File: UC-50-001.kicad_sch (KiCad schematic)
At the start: 0 parts

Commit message: RAM : temporairement fini
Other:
- sheet RAM renamed I02–05–07–08–09–11–12–17–19–23–RAM
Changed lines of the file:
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@@
     (stroke (width 0.1524) (type solid) (color 0 0 0 0))
     (fill (color 0 0 0 0.0000))
-    (property "Sheet name" "RAM" (id 0) (at 30.48 76.4934 0)
+    (property "Sheet name" "I02–05–07–08–09–11–12–17–19–23–RAM" (id 0) (at 30.48 76.4934 0)
       (effects (font (size 1.8 1.8)) (justify left bottom))
     )
@@
       (reference "#PWR?") (unit 1) (value "GND") (footprint "")
     )
+    (path "/3b9df46e-3592-4470-9765-1c36c3c4b1c2/0c08bfbe-48ca-4db2-92f3-dc7b8238d261"
+      (reference "#PWR?") (unit 1) (value "GND") (footprint "")
+    )
     (path "/f465a4b1-7c3c-40cc-9e66-ff9f17003d42/0f6a8f7c-8ebc-48ff-a299-e91c43441b34"
       (reference "#PWR?") (unit 1) (value "GND") (footprint "")
@@
       (reference "#PWR?") (unit 1) (value "+5V") (footprint "")
     )
+    (path "/3b9df46e-3592-4470-9765-1c36c3c4b1c2/7435153a-c468-4d7b-8502-3365d7ea767d"
+      (reference "#PWR?") (unit 1) (value "+5V") (footprint "")
+    )
     (path "/afd59d07-bfd6-4bc9-8176-e0ddec1872a1/76921501-701f-4c1f-8225-7bfdc888d467"
       (reference "#PWR?") (unit 1) (value "GND") (footprint "")
@@
       (reference "#PWR?") (unit 1) (value "GND") (footprint "")
     )
+    (path "/3b9df46e-3592-4470-9765-1c36c3c4b1c2/89541933-c7ab-4d42-acee-72bf689ebaa3"
+      (reference "#PWR?") (unit 1) (value "GND") (footprint "")
+    )
     (path "/b7e71b61-5858-491f-a12d-087d8cf2d648/8bd665a3-d2bc-4eb9-ab07-d1b073552cd5"
       (reference "#PWR?") (unit 1) (value "+5V") (footprint "")
@@
       (reference "#PWR?") (unit 1) (value "GND") (footprint "")
     )
+    (path "/3b9df46e-3592-4470-9765-1c36c3c4b1c2/9b2f435e-c9f5-4022-a643-0a2a885f898c"
+      (reference "#PWR?") (unit 1) (value "GND") (footprint "")
+    )
     (path "/afd59d07-bfd6-4bc9-8176-e0ddec1872a1/9b9e676b-a45e-44f0-8f14-e409b9618c02"
       (reference "#PWR?") (unit 1) (value "GND") (footprint "")
     )
+    (path "/3b9df46e-3592-4470-9765-1c36c3c4b1c2/9bd4cdcc-9b91-440c-8f95-cc6edf9cc717"
+      (reference "#PWR?") (unit 1) (value "+5V") (footprint "")
+    )
     (path "/3b9df46e-3592-4470-9765-1c36c3c4b1c2/a00adc77-b775-4350-9b35-84be2bc872bc"
       (reference "#PWR?") (unit 1) (value "GND") (footprint "")
@@
       (reference "#PWR?") (unit 1) (value "+5V") (footprint "")
     )
+    (path "/3b9df46e-3592-4470-9765-1c36c3c4b1c2/bd8749e0-1840-4927-bb4e-27bf2d69b91e"
+      (reference "#PWR?") (unit 1) (value "+5V") (footprint "")
+    )
     (path "/3b9df46e-3592-4470-9765-1c36c3c4b1c2/bde68ce5-ebc7-4aa3-8add-c6386f0e31b1"
       (reference "#PWR?") (unit 1) (value "GND") (footprint "")
@@
       (reference "#PWR?") (unit 1) (value "+5V") (footprint "")
     )
+    (path "/3b9df46e-3592-4470-9765-1c36c3c4b1c2/c8f86357-7c56-49dd-841f-0b8016155e76"
+      (reference "#PWR?") (unit 1) (value "GND") (footprint "")
+    )
     (path "/b7e71b61-5858-491f-a12d-087d8cf2d648/cc2f772d-66f5-4ef2-bf72-bf4cabe8468e"
       (reference "#PWR?") (unit 1) (value "GND") (footprint "")
@@
     )
     (path "/3b9df46e-3592-4470-9765-1c36c3c4b1c2/d74e7404-2964-4604-a79a-633d2f0c5c76"
+      (reference "#PWR?") (unit 1) (value "GND") (footprint "")
+    )
+    (path "/3b9df46e-3592-4470-9765-1c36c3c4b1c2/d85bd63e-ddec-4520-b1c2-47b8d0d2c25a"
+      (reference "#PWR?") (unit 1) (value "GND") (footprint "")
+    )
+    (path "/3b9df46e-3592-4470-9765-1c36c3c4b1c2/dd1a7648-1801-4481-97bd-fb427a294716"
       (reference "#PWR?") (unit 1) (value "GND") (footprint "")
     )
@@
       (reference "C01") (unit 1) (value "100uF") (footprint "")
     )
+    (path "/3b9df46e-3592-4470-9765-1c36c3c4b1c2/e7011fa1-0a2a-4048-a729-5a3912728b22"
+      (reference "C02") (unit 1) (value "100pF") (footprint "")
+    )
+    (path "/3b9df46e-3592-4470-9765-1c36c3c4b1c2/5c0ace55-ad46-4721-b2a9-13c47105194e"
+      (reference "C03") (unit 1) (value "100pF") (footprint "")
+    )
     (path "/b7e71b61-5858-491f-a12d-087d8cf2d648/36dce4c7-2705-4bcb-b676-3fb13d1e9187"
       (reference "C7") (unit 1) (value "220nF") (footprint "")
@@
       (reference "C31") (unit 1) (value "47nF") (footprint "")
     )
+    (path "/3b9df46e-3592-4470-9765-1c36c3c4b1c2/df1775be-95fd-4d6c-9689-ecaeb7ae759a"
+      (reference "C33") (unit 1) (value "47nF") (footprint "")
+    )
     (path "/3b9df46e-3592-4470-9765-1c36c3c4b1c2/04c98286-549c-4582-8a40-dd933b3c8a44"
       (reference "C35") (unit 1) (value "47nF") (footprint "")
@@
       (reference "C?") (unit 1) (value "100uF") (footprint "")
     )
+    (path "/3b9df46e-3592-4470-9765-1c36c3c4b1c2/4393184f-e494-46f3-b5c4-6143e8e72043"
+      (reference "C?") (unit 1) (value "47nF") (footprint "")
+    )
     (path "/3b9df46e-3592-4470-9765-1c36c3c4b1c2/76e33095-d5c1-4315-9b36-4ce1828dbef6"
       (reference "C?") (unit 1) (value "10nF") (footprint "")
@@
       (reference "C?") (unit 1) (value "47nF") (footprint "")
     )
-    (path "/3b9df46e-3592-4470-9765-1c36c3c4b1c2/df1775be-95fd-4d6c-9689-ecaeb7ae759a"
+    (path "/3b9df46e-3592-4470-9765-1c36c3c4b1c2/f3d75b2b-a10e-400b-95b7-25d1a994b88f"
       (reference "C?") (unit 1) (value "47nF") (footprint "")
     )
@@
       (reference "I08") (unit 1) (value "TMS4416 – 16k×4bits DRAM") (footprint "Package_DIP:DIP-18_W7.62mm_LongPads")
     )
+    (path "/3b9df46e-3592-4470-9765-1c36c3c4b1c2/e5b33663-4b58-4516-8cd9-ab2a59a9d103"
+      (reference "I09") (unit 1) (value "74LS32 – 4× 2-input OR gates") (footprint "Package_DIP:DIP-14_W7.62mm_LongPads")
+    )
     (path "/3b9df46e-3592-4470-9765-1c36c3c4b1c2/edf7d0d1-1070-4c87-a709-1d85f3bb622c"
       (reference "I11") (unit 1) (value "TMS4416 – 16k×4bits DRAM") (footprint "Package_DIP:DIP-18_W7.62mm_LongPads")
     )
+    (path "/3b9df46e-3592-4470-9765-1c36c3c4b1c2/5544af09-10f1-4418-a4ab-05a6362d4390"
+      (reference "I12") (unit 1) (value "74LS11 – 3×3 inputs AND gates") (footprint "Package_DIP:DIP-14_W7.62mm_LongPads")
+    )
     (path "/3b9df46e-3592-4470-9765-1c36c3c4b1c2/72e2b5de-308f-467f-abcc-77d273bcfa07"
       (reference "I17") (unit 1) (value "74LS245 – Bus transceiver") (footprint "Package_DIP:DIP-20_W7.62mm_LongPads")
@@
       (reference "R13") (unit 1) (value "3K3") (footprint "")
     )
+    (path "/3b9df46e-3592-4470-9765-1c36c3c4b1c2/7cc7717b-b384-4c56-8c71-316373184291"
+      (reference "R29") (unit 1) (value "100") (footprint "")
+    )
     (path "/f465a4b1-7c3c-40cc-9e66-ff9f17003d42/86aa1ccc-5151-4ba7-a26f-79b9e96ed260"
       (reference "R31") (unit 1) (value "1K") (footprint "")
@@
       (reference "R33") (unit 1) (value "1K") (footprint "")
     )
+    (path "/3b9df46e-3592-4470-9765-1c36c3c4b1c2/9c7d7f95-2f97-474d-ae54-bf4c023ef25b"
+      (reference "R34") (unit 1) (value "100") (footprint "")
+    )
     (path "/b7e71b61-5858-491f-a12d-087d8cf2d648/f6934876-7f17-4d7e-bec9-35b9ebc47134"

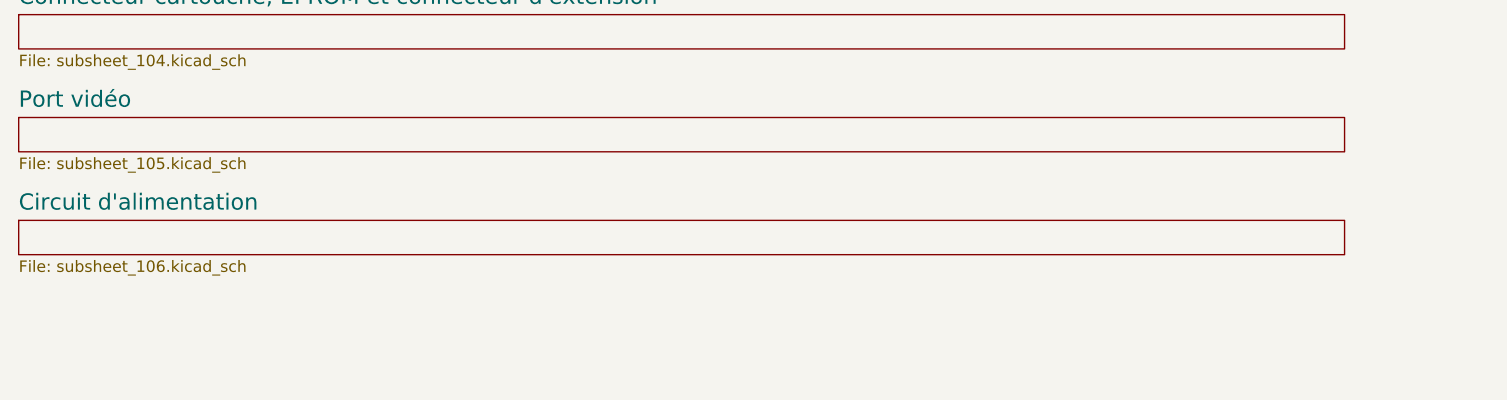
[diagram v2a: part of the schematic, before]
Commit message: provisionne une feuille pour le système d'horloges
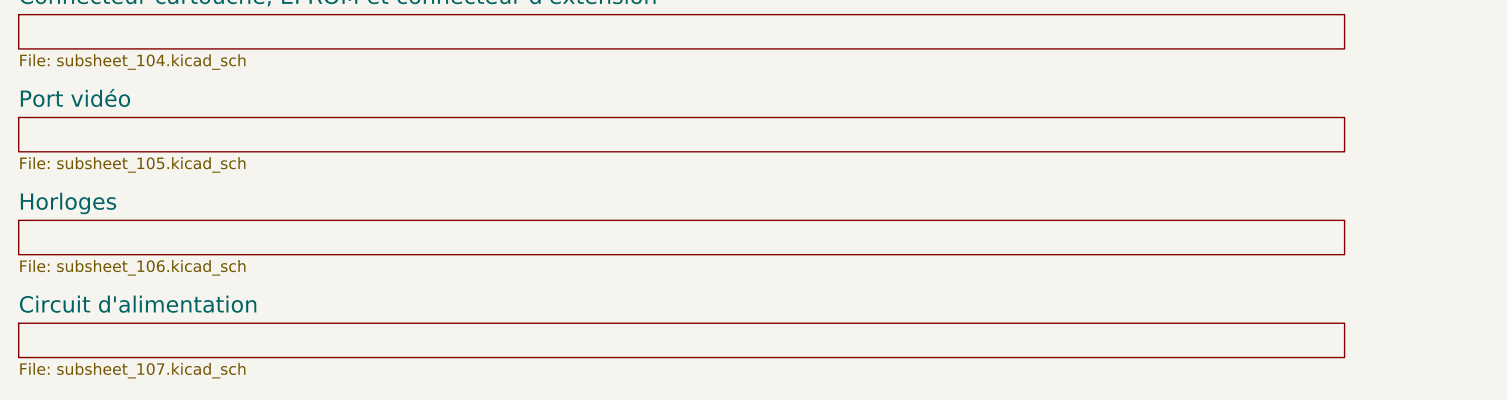
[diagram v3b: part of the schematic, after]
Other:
- added sheet Horloges (subsheet_106.kicad_sch)
- sheet Circuit d'alimentation: file subsheet_106.kicad_sch -> subsheet_107.kicad_sch
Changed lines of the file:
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@@
     (stroke (width 0.1524) (type solid) (color 0 0 0 0))
     (fill (color 0 0 0 0.0000))
-    (property "Sheet name" "Circuit d'alimentation" (id 0) (at 30.48 122.2134 0)
+    (property "Sheet name" "Horloges" (id 0) (at 30.48 122.2134 0)
       (effects (font (size 1.8 1.8)) (justify left bottom))
     )
     (property "Sheet file" "subsheet_106.kicad_sch" (id 1) (at 30.48 127.5846 0)
+      (effects (font (size 1.27 1.27)) (justify left top))
+    )
+  )
+  (sheet (at 30.48 134.62) (size 147.32 3.81) (fields_autoplaced)
+    (stroke (width 0.1524) (type solid) (color 0 0 0 0))
+    (fill (color 0 0 0 0.0000))
+    (property "Sheet name" "Circuit d'alimentation" (id 0) (at 30.48 133.6434 0)
+      (effects (font (size 1.8 1.8)) (justify left bottom))
+    )
+    (property "Sheet file" "subsheet_107.kicad_sch" (id 1) (at 30.48 139.0146 0)
       (effects (font (size 1.27 1.27)) (justify left top))
     )
@@
     (path "/10b20128-1f32-45c7-94f3-33002744903c" (page "7"))
     (path "/706ec47c-3d4a-4bde-bb8b-c4f8dcc96c45" (page "8"))
+    (path "/86f44e2a-9fb4-43d0-b64c-d20135fe820e" (page "9"))
   )
   (symbol_instances

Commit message: remise au propre
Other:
- sheet Circuit d'alimentation renamed I54–55–Circuit d'alimentation +18V vers +5V
- sheet I48–MC6821P - ports clavier, crayon optique et LEP renamed I48–MC6821P ; I52–53–B04–B05–ports clavier ; PM01–LEP ; PM02–Crayon optique
- title: Conversion du Thomson MO5 — Unité centrale -> Conversion du Thomson MO5 — Unité centrale v1
